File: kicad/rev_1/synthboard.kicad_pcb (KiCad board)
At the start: 2 copper layers, 133.3 x 55.2 mm, 51 parts, among them J1 Connect to Upper Module/Mothe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, J2 Connect to Lower Module, J3 Modular Inputs, SW1 SW_Push, SW10 SW_Push, SW11 SW_Push, SW12 SW_Push, SW2 SW_Push, SW3 SW_Push, SW4 SW_Push, SW5 SW_Push, SW6 SW_Push, SW7 SW_Push, SW8 SW_Push, SW9 SW_Push, U1 74HC165, U2 74HC165

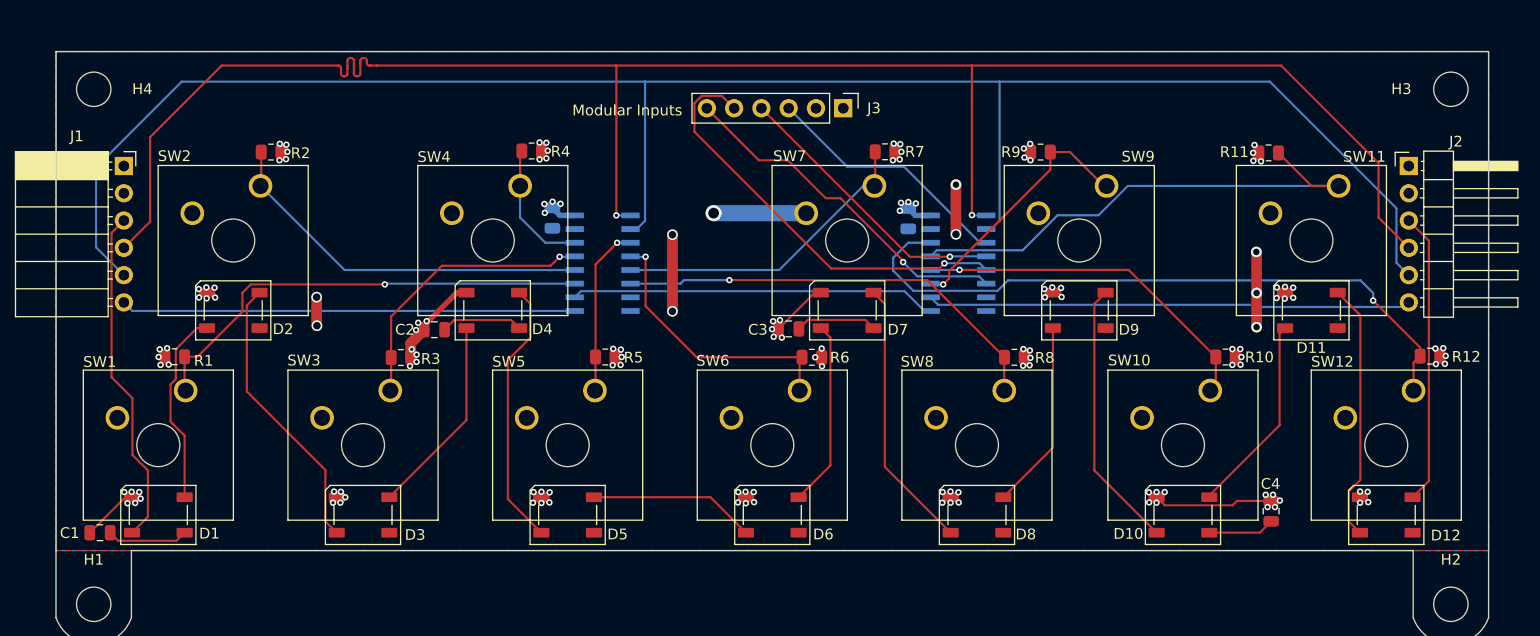
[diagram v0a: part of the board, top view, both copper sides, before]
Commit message: Added Text to PCB & Updated README
Added informational text to PCB, including designer names, board name, and revision number.

Improved quality of the PCB Image by screenshotting the KiCad 3D viewer instead of using the native export function.
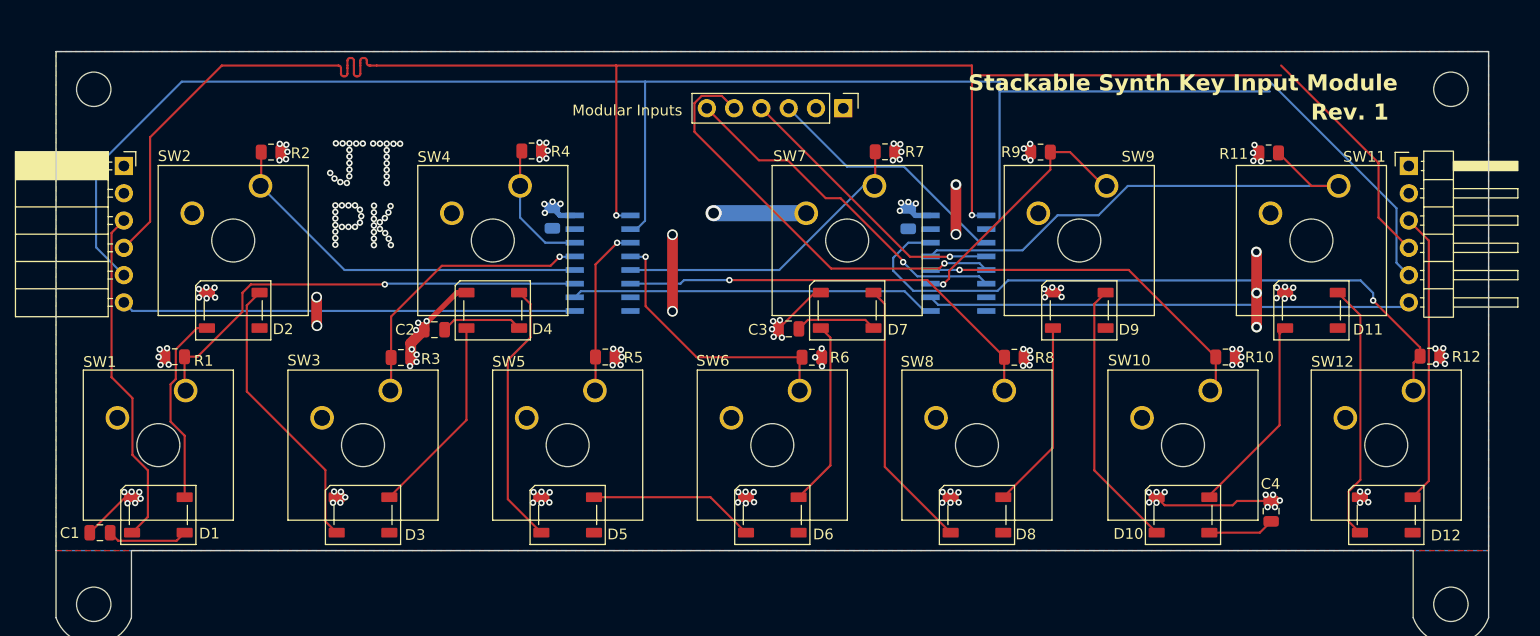
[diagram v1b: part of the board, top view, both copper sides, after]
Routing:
- net GND: vias 132 -> 147
- net +5V: vias 9 -> 50
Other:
- board text added: "Designed by: • Jesse Thompson • Peter Kyle"
- board text added: "Rev. 1"
- board text added: "Stackable Synth Key Input Module"

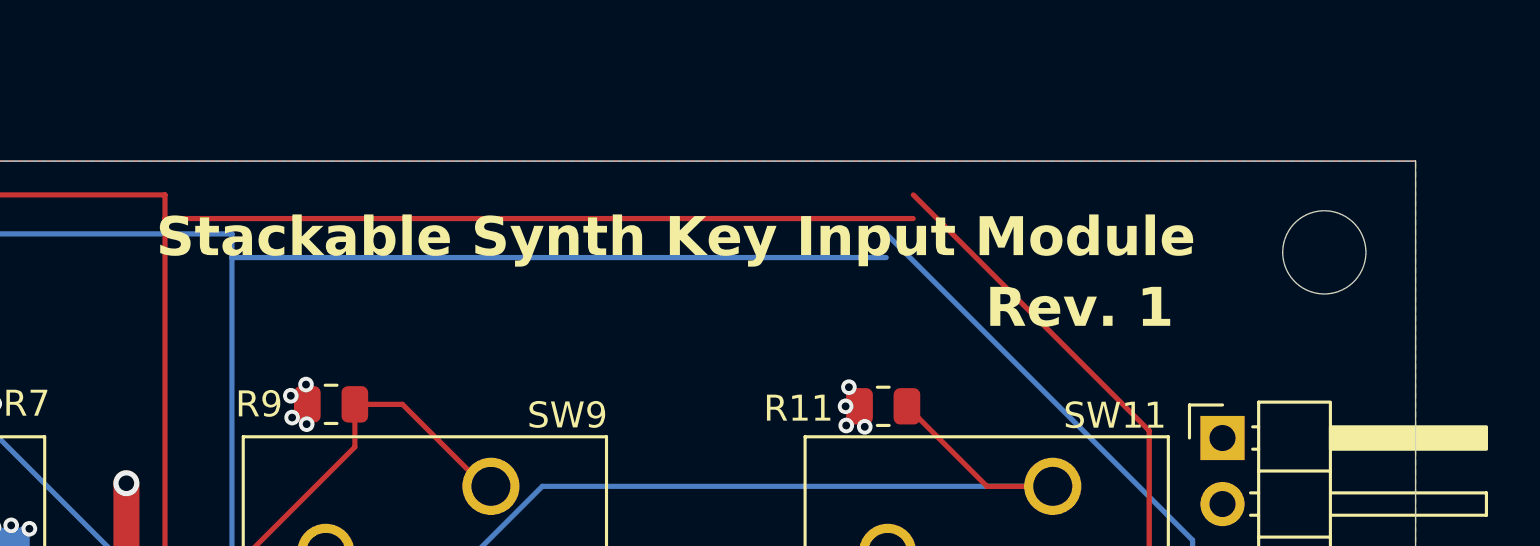
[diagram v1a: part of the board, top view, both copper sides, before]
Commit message: PCB updates
edited silkscreen and generated final production files for JLCPCB
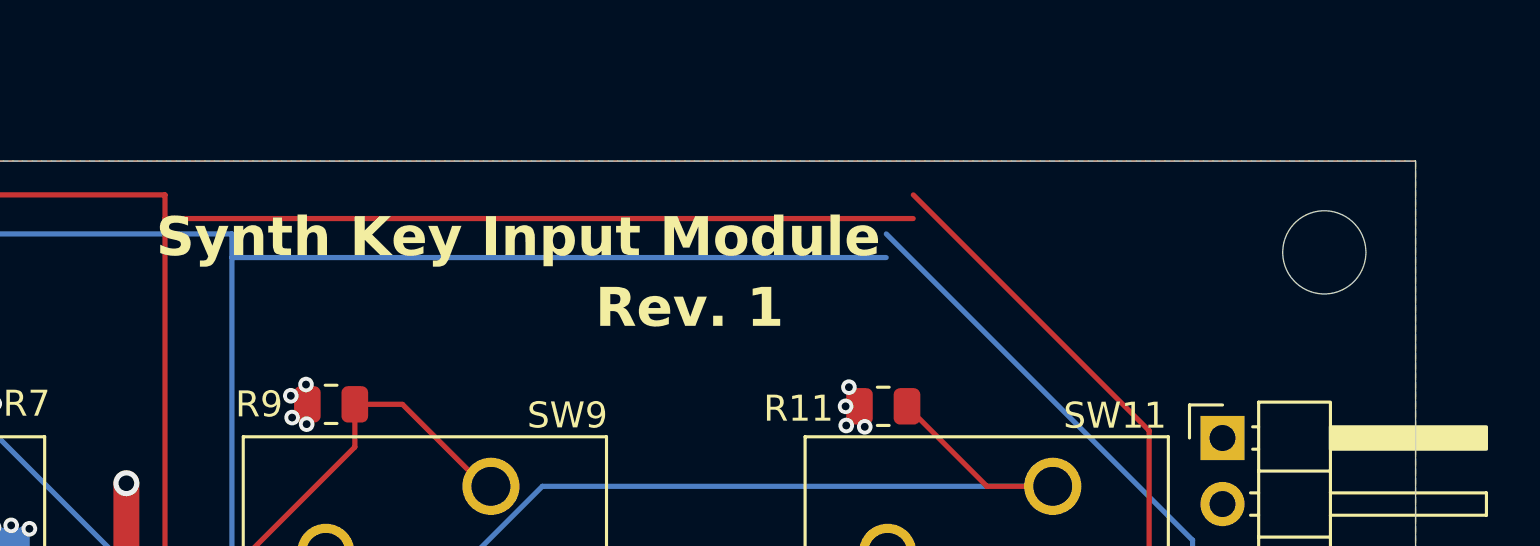
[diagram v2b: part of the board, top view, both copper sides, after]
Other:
- board text added: "Synth Key Input Module"
- board text removed: "Stackable Synth Key Input Module"
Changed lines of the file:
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@@
+	)
+	(gr_line
+		(start 41.6 128.378403)
+		(end 41.6 112.96)
+		(stroke
+			(width 0.1)
+			(type default)
+		)
+		(layer "Dwgs.User")
 	)
 	(gr_line
@@
 		)
 	)
-	(gr_text "Stackable Synth Key Input Module"
+	(gr_text "Synth Key Input Module"
 		(at 124.28 107.5 0)
 		(layer "F.SilkS")
@@
 	)
 	(gr_text "Rev. 1"
-		(at 156.175 110.22 0)
+		(at 141.175 110.22 0)
 		(layer "F.SilkS")
 		(effects
@@
 	)
 	(gr_text "Rev. 1"
-		(at 132.005 110.22 -0)
+		(at 145.005 110.22 0)
 		(layer "B.SilkS")
 		(effects
@@
 		)
 	)
-	(gr_text "Stackable Synth Key Input Module"
-		(at 164.145 107.63 -0)
+	(gr_text "Synth Key Input Module"
+		(at 164.145 107.63 0)
 		(layer "B.SilkS")
 		(effects
@@
 		)
 	)
+	(dimension
+		(type orthogonal)
+		(layer "Dwgs.User")
+		(pts
+			(xy 175.445 127.48) (xy 172.72 127.48)
+		)
+		(height 2.48)
+		(orientation 0)
+		(format
+			(prefix "")
+			(suffix "")
+			(units 3)
+			(units_format 0)
+			(precision 4)
+			(suppress_zeroes yes)
+		)
+		(style
+			(thickness 0.1)
+			(arrow_length 1.27)
+			(text_position_mode 0)
+			(arrow_direction outward)
+			(extension_height 0.58642)
+			(extension_offset 0.5)
+			(keep_text_aligned yes)
+		)
+		(gr_text "2.725"
+			(at 174.0825 128.81 0)
+			(layer "Dwgs.User")
+			(effects
+				(font
+					(size 1 1)
+					(thickness 0.15)
+				)
+			)
+		)
+	)
+	(dimension
+		(type orthogonal)
+		(layer "Dwgs.User")
+		(pts
+			(xy 35.595 123.24) (xy 39.37 123.24)
+		)
+		(height 0)
+		(orientation 0)
+		(format
+			(prefix "")
+			(suffix "")
+			(units 3)
+			(units_format 0)
+			(precision 4)
+			(suppress_zeroes yes)
+		)
+		(style
+			(thickness 0.1)
+			(arrow_length 1.27)
+			(text_position_mode 0)
+			(arrow_direction outward)
+			(extension_height 0.58642)
+			(extension_offset 0.5)
+			(keep_text_aligned yes)
+		)
+		(gr_text "3.775"
+			(at 37.4825 122.09 0)
+			(layer "Dwgs.User")
+			(effects
+				(font
+					(size 1 1)
+					(thickness 0.15)
+				)
+			)
+		)
+	)
+	(dimension
+		(type orthogonal)
+		(layer "Dwgs.User")
+		(pts
+			(xy 35.595 125.78) (xy 41.6 125.78)
+		)
+		(height 1.145)
+		(orientation 0)
+		(format
+			(prefix "")
+			(suffix "")
+			(units 3)
+			(units_format 0)
+			(precision 4)
+			(suppress_zeroes yes)
+		)
+		(style
+			(thickness 0.1)
+			(arrow_length 1.27)
+			(text_position_mode 0)
+			(arrow_direction outward)
+			(extension_height 0.58642)
+			(extension_offset 0.5)
+			(keep_text_aligned yes)
+		)
+		(gr_text "6.005"
+			(at 38.5975 125.775 0)
+			(layer "Dwgs.User")
+			(effects
+				(font
+					(size 1 1)
+					(thickness 0.15)
+				)
+			)
+		)
+	)
+	(dimension
+		(type orthogonal)
+		(layer "Dwgs.User")
+		(pts
+			(xy 41.6 120.669202) (xy 39.37 120.7)
+		)
+		(height -1.039202)
+		(orientation 0)
+		(format
+			(prefix "")
+			(suffix "")
+			(units 3)
+			(units_format 0)
+			(precision 4)
+			(suppress_zeroes yes)
+		)
+		(style
+			(thickness 0.1)
+			(arrow_length 1.27)
+			(text_position_mode 0)
+			(arrow_direction outward)
+			(extension_height 0.58642)
+			(extension_offset 0.5)
+			(keep_text_aligned yes)
+		)
+		(gr_text "2.23"
+			(at 40.485 118.48 0)
+			(layer "Dwgs.User")
+			(effects
+				(font
+					(size 1 1)
+					(thickness 0.15)
+				)
+			)
+		)
+	)
